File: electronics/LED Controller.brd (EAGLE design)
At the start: 35.6 x 48.3 mm, 20 parts, among them J1 1-770968-0, J2 DF1BZ-8DP-2.5DSA, J3 LED8, J4 LED16, U1 MCP23S08-E/SO, U2 ATMEGA328PB32-TQFP, U3 MCP23S17T-E/SO

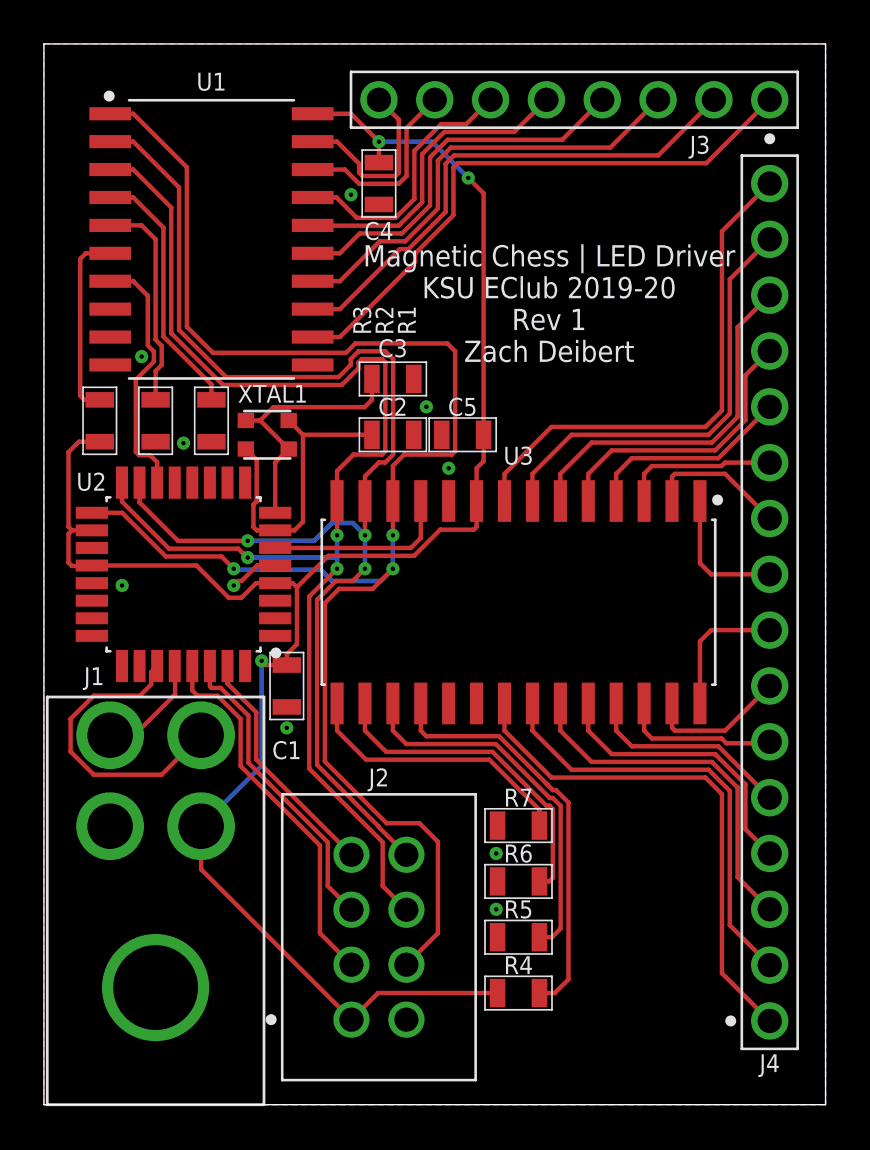
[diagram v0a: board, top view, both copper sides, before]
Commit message: Added current-limiting resistors for LEDs
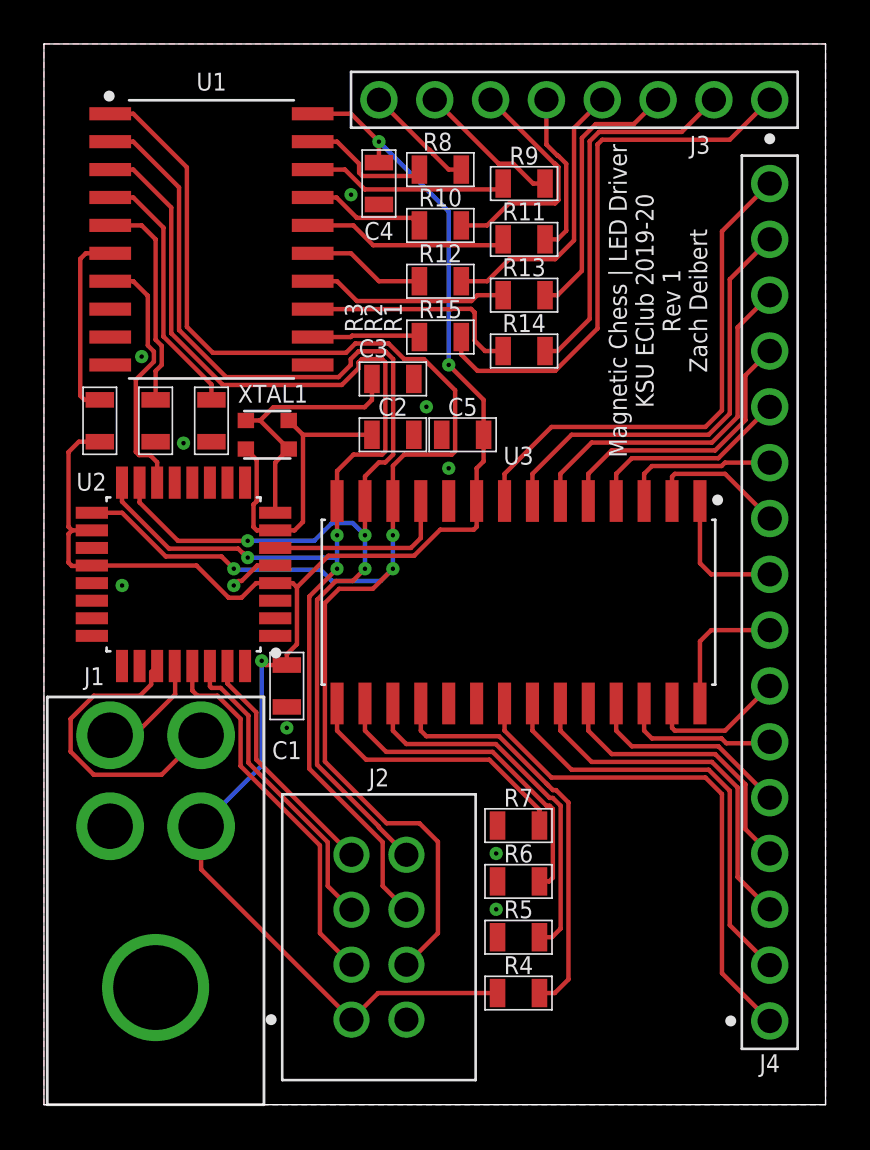
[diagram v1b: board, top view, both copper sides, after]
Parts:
- added R10, R11, R12, R13, R14, R15, R8, R9: (no value), Zach:0805
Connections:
- new net N$10: R10.P$2, U1.17
- new net N$11: R11.P$2, U1.16
- new net N$12: R12.P$2, U1.15
- new net N$13: R13.P$2, U1.14
- new net N$14: R14.P$2, U1.13
- new net N$15: R15.P$2, U1.12
- new net N$8: R8.P$2, U1.19
- new net N$9: R9.P$2, U1.18
- net A: now also R15.P$1; no longer U1.12
- net B: now also R14.P$1; no longer U1.13
- net C: now also R13.P$1; no longer U1.14
- net D: now also R12.P$1; no longer U1.15
- net E: now also R11.P$1; no longer U1.16
- net F: now also R10.P$1; no longer U1.17
- net G: now also R9.P$1; no longer U1.18
- net H: now also R8.P$1; no longer U1.19
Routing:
- net N$14: track 0.00 -> 10.2 mm
- net N$13: track 0.00 -> 9.15 mm
- net N$11: track 0.00 -> 9.15 mm
- net N$9: track 0.00 -> 9.15 mm
- net C: track 20.4 -> 12.4 mm
- net E: track 14.3 -> 7.48 mm
- net B: track 23.5 -> 17.2 mm
- net N$8: track 0.00 -> 5.86 mm
- net N$12: track 0.00 -> 5.38 mm
- net N$10: track 0.00 -> 5.38 mm
- net N$15: track 0.00 -> 4.91 mm
- net D: track 17.3 -> 12.8 mm
- net H: track 8.56 -> 5.08 mm
- net G: track 8.69 -> 6.59 mm
- net A: track 26.8 -> 25.2 mm
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
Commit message: Added pull-up on RESET
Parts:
- added R16: 10k, Zach:0805
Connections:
- net !RESET: now also R16.P$1
- net +3V3: now also R16.P$2
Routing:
- net !RESET: track 17.1 -> 25.4 mm
- net +3V3: track 84.9 -> 92.3 mm
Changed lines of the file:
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@@
 <attribute name="NAME" x="18.034" y="36.6014" size="0.8128" layer="25" rot="R180" align="bottom-center"/>
+</element>
+<element name="R16" library="Zach" package="0805" value="10k" x="21.59" y="2.54" smashed="yes">
+<attribute name="NAME" x="21.59" y="3.4036" size="0.8128" layer="25" align="bottom-center"/>
 </element>
 </elements>
@@
 <wire x1="11.5099" y1="20.9512375" x2="11.5099" y2="23.5421" width="0.2032" layer="1"/>
 <wire x1="11.322" y1="23.73" x2="11.5099" y2="23.5421" width="0.2032" layer="1"/>
-<wire x1="20.6375" y1="5.08" x2="15.2" y2="5.08" width="0.2032" layer="1"/>
-<wire x1="15.2" y1="5.08" x2="13.99" y2="3.87" width="0.2032" layer="1"/>
 <wire x1="13.99" y1="3.87" x2="7.15" y2="10.71" width="0.2032" layer="1"/>
 <wire x1="7.15" y1="10.71" x2="7.15" y2="12.67" width="0.2032" layer="1"/>
@@
 <wire x1="18.415" y1="33.655" x2="18.415" y2="40.64" width="0.2032" layer="16"/>
 <wire x1="18.415" y1="40.64" x2="15.24" y2="43.815" width="0.2032" layer="16"/>
+<contactref element="R16" pad="P$2"/>
+<wire x1="13.99" y1="3.87" x2="16.2217" y2="1.6383" width="0.2032" layer="1"/>
+<wire x1="22.5425" y1="1.7145" x2="22.5425" y2="2.54" width="0.2032" layer="1"/>
+<wire x1="16.2217" y1="1.6383" x2="22.4663" y2="1.6383" width="0.2032" layer="1"/>
+<wire x1="22.4663" y1="1.6383" x2="22.5425" y2="1.7145" width="0.2032" layer="1"/>
+<wire x1="22.5425" y1="2.54" x2="21.844" y2="2.54" width="0.2032" layer="1"/>
+<wire x1="21.844" y1="2.54" x2="21.59" y2="2.794" width="0.2032" layer="1"/>
+<wire x1="21.59" y1="4.826" x2="21.336" y2="5.08" width="0.2032" layer="1"/>
+<wire x1="21.336" y1="5.08" x2="20.6375" y2="5.08" width="0.2032" layer="1"/>
+<wire x1="21.59" y1="2.794" x2="21.59" y2="4.826" width="0.2032" layer="1"/>
 </signal>
 <signal name="GND">
@@
 <wire x1="12.5554" y1="7.8046" x2="13.99" y2="6.37" width="0.2032" layer="1"/>
 <wire x1="12.5554" y1="11.7988" x2="12.5554" y2="7.8046" width="0.2032" layer="1"/>
+<contactref element="R16" pad="P$1"/>
+<wire x1="20.6375" y1="2.54" x2="19.3459375" y2="2.54" width="0.2032" layer="1"/>
+<wire x1="15.411" y1="4.949" x2="13.99" y2="6.37" width="0.2032" layer="1"/>
+<wire x1="19.3459375" y1="2.54" x2="16.9369375" y2="4.949" width="0.2032" layer="1"/>
+<wire x1="16.9369375" y1="4.949" x2="15.411" y2="4.949" width="0.2032" layer="1"/>
 </signal>
 <signal name="XTAL2">

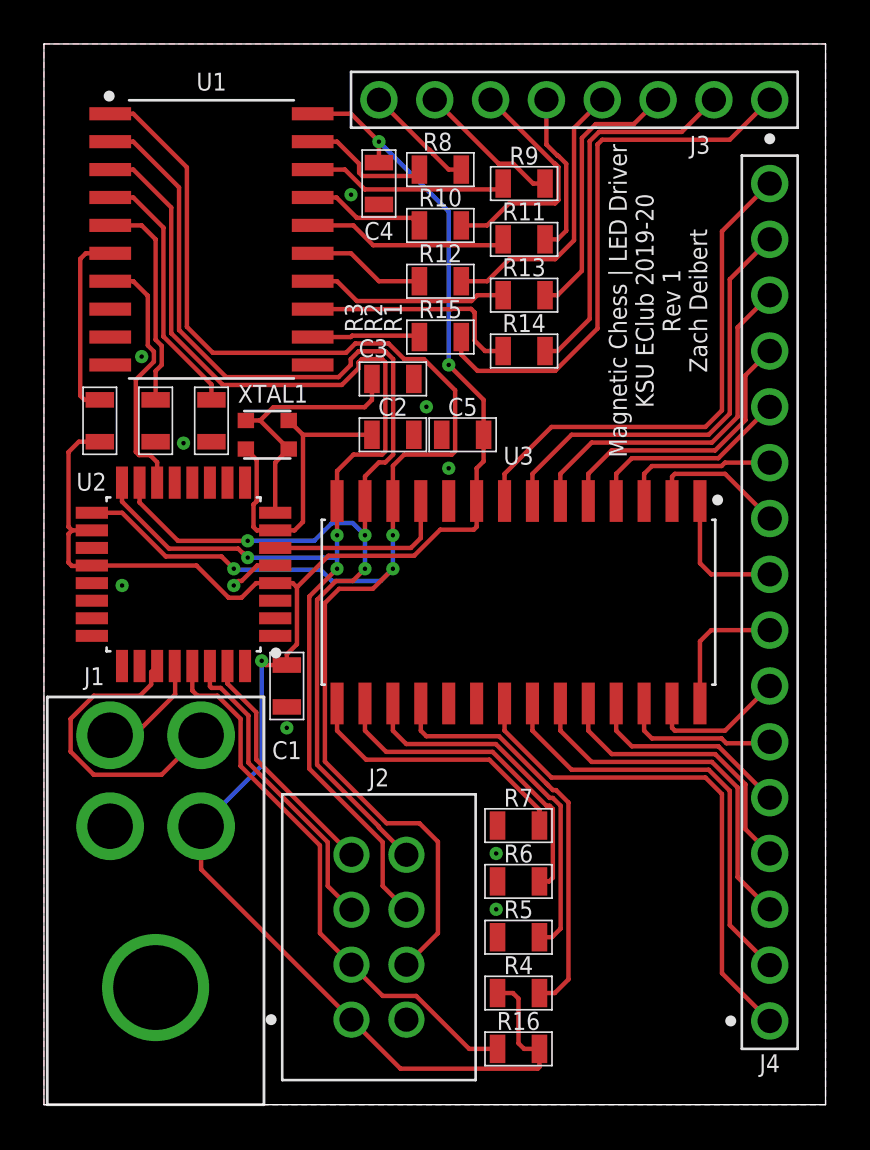
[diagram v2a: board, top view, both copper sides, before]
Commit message: Added mounting holes
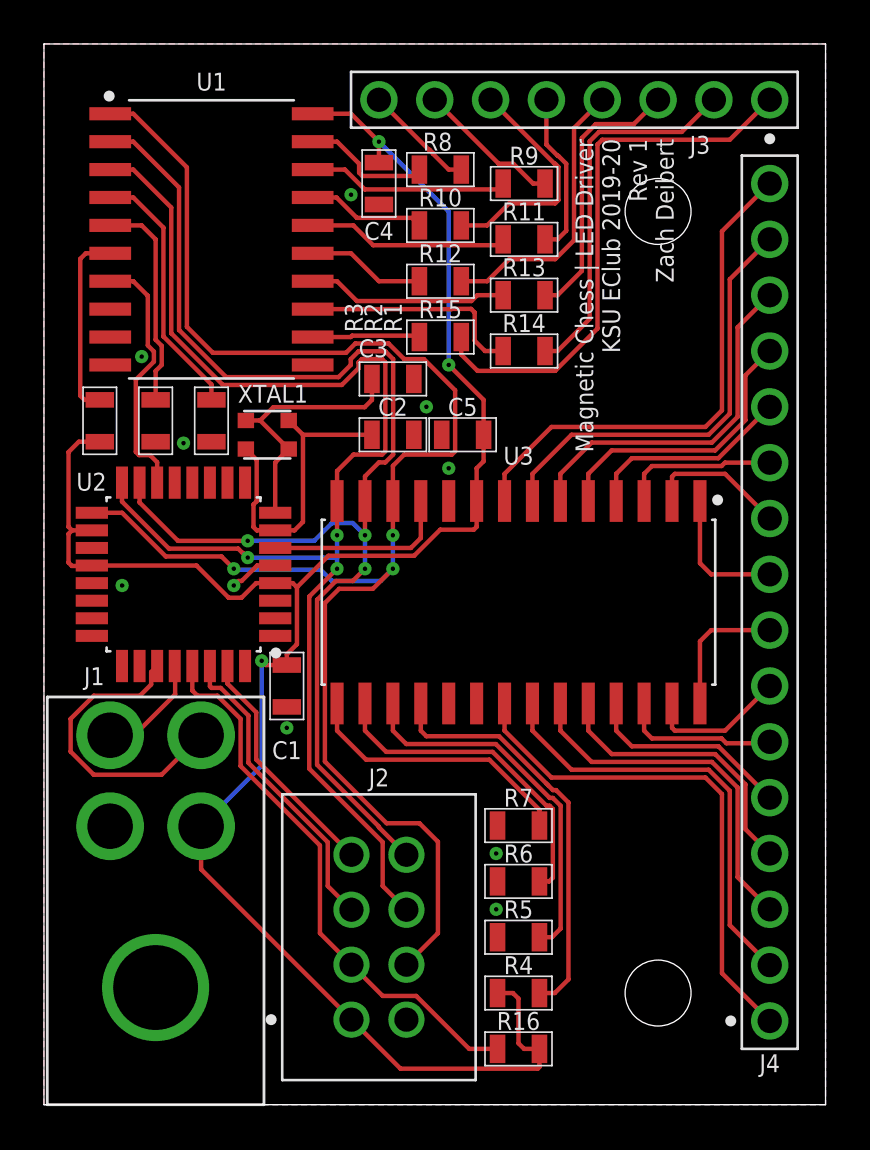
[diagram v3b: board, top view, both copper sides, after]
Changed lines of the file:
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@@
 <setting verticaltext="up"/>
 </settings>
-<grid distance="5" unitdist="mil" unit="mil" style="lines" multiple="1" display="no" altdistance="5" altunitdist="mil" altunit="mil"/>
+<grid distance="50" unitdist="mil" unit="mil" style="lines" multiple="1" display="no" altdistance="5" altunitdist="mil" altunit="mil"/>
 <layers>
 <layer number="1" name="Top" color="4" fill="1" visible="yes" active="yes"/>
@@
 <layer number="27" name="tValues" color="7" fill="1" visible="yes" active="yes"/>
 <layer number="28" name="bValues" color="7" fill="1" visible="yes" active="yes"/>
-<layer number="29" name="tStop" color="7" fill="3" visible="no" active="yes"/>
-<layer number="30" name="bStop" color="7" fill="6" visible="no" active="yes"/>
+<layer number="29" name="tStop" color="7" fill="3" visible="yes" active="yes"/>
+<layer number="30" name="bStop" color="7" fill="6" visible="yes" active="yes"/>
 <layer number="31" name="tCream" color="7" fill="4" visible="no" active="yes"/>
 <layer number="32" name="bCream" color="7" fill="5" visible="no" active="yes"/>
@@
 <layer number="43" name="vRestrict" color="2" fill="10" visible="yes" active="yes"/>
 <layer number="44" name="Drills" color="7" fill="1" visible="no" active="yes"/>
-<layer number="45" name="Holes" color="7" fill="1" visible="no" active="yes"/>
+<layer number="45" name="Holes" color="7" fill="1" visible="yes" active="yes"/>
 <layer number="46" name="Milling" color="3" fill="1" visible="no" active="yes"/>
 <layer number="47" name="Measures" color="7" fill="1" visible="no" active="yes"/>
@@
 <wire x1="35.56" y1="48.26" x2="0" y2="48.26" width="0" layer="20"/>
 <wire x1="0" y1="48.26" x2="0" y2="0" width="0" layer="20"/>
-<text x="27.94" y="36.576" size="0.8128" layer="21" rot="R270" align="center">Magnetic Chess | LED Driver
+<text x="26.416" y="43.942" size="0.8128" layer="21" rot="R270" align="center-left">Magnetic Chess | LED Driver
 KSU EClub 2019-20
 Rev 1
 Zach Deibert</text>
+<hole x="27.94" y="40.64" drill="3"/>
+<hole x="27.94" y="5.08" drill="3"/>
 </plain>
 <attributes>
